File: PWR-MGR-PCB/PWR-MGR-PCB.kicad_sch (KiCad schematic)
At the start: 24 parts, among them J1 USB_C_Receptacle_USB2.0_14P, J2 Battery_1x2, U1 USBLC6-2SC6, U2 TLV75533PDBV, U3 BQ24074RGT, U4 TPS631011YBGR

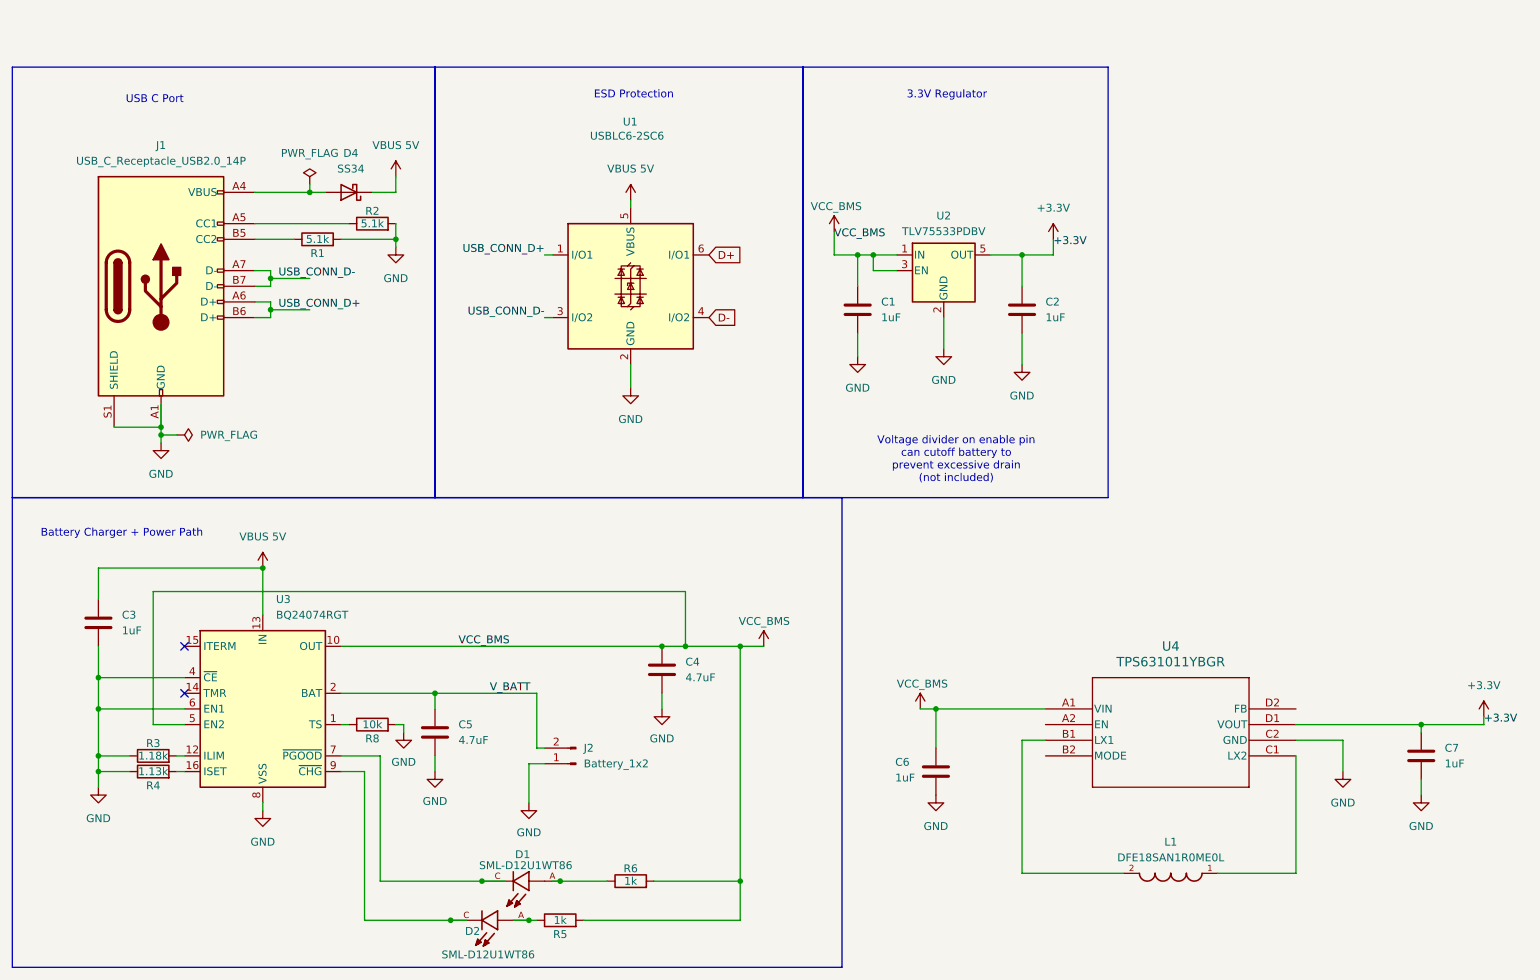
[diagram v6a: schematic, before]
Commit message: Configure buck boost converter
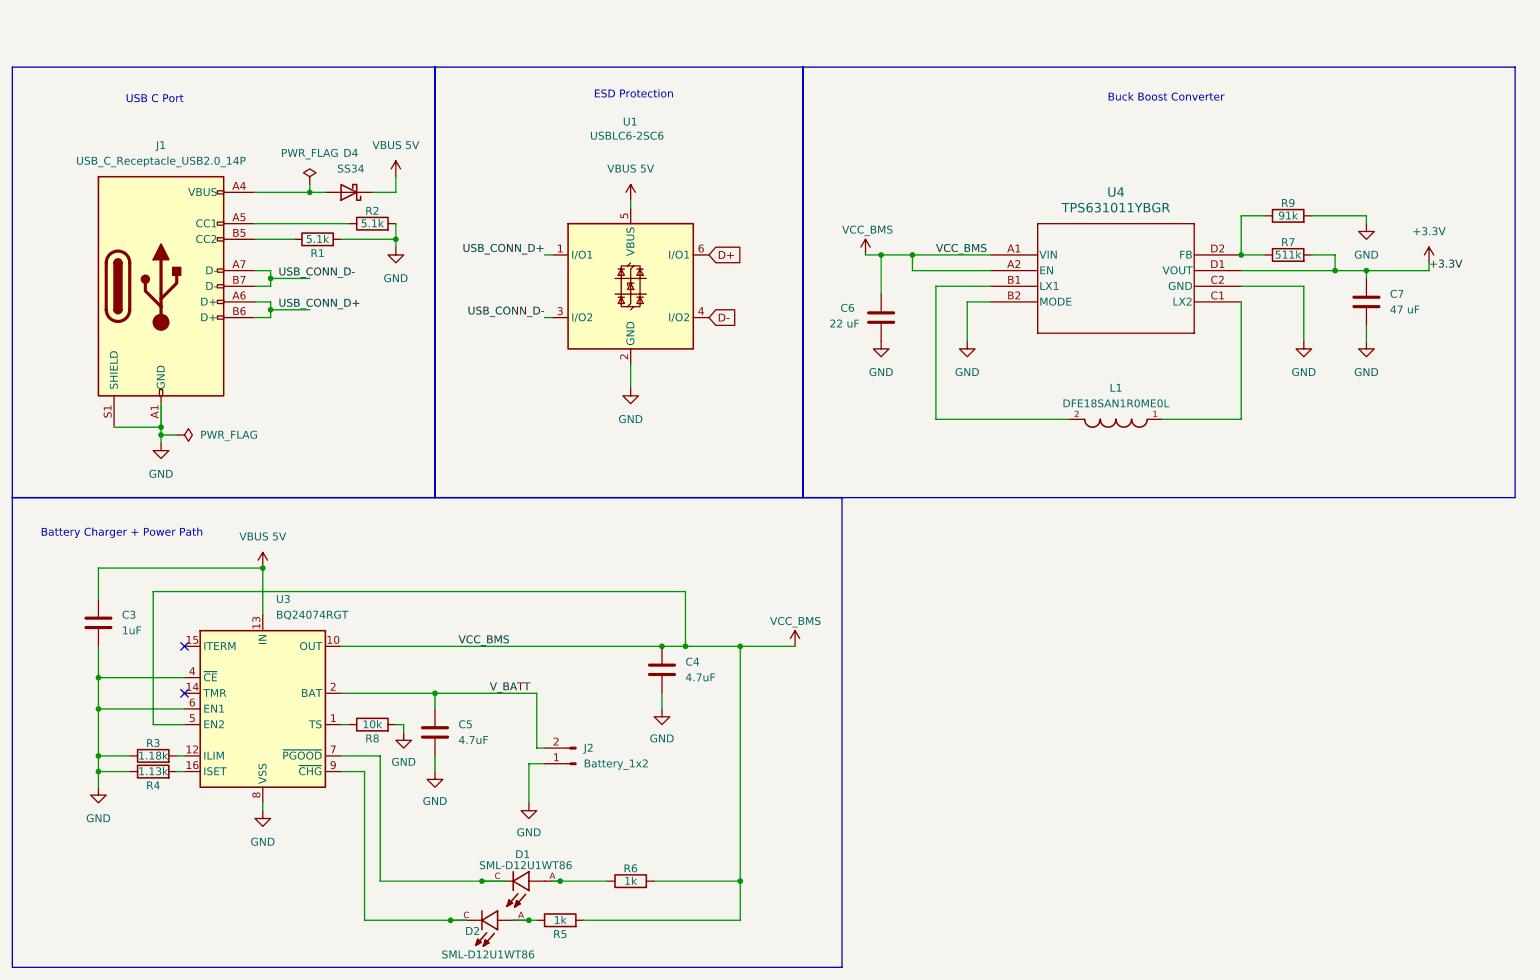
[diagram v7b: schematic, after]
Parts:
- removed C1, C2: 1uF, Capacitor_SMD:C_0805_2012Metric, symbol Device:C
- removed U2: TLV75533PDBV, Package_TO_SOT_SMD:SOT-23-5, symbol Regulator_Linear:TLV75533PDBV
- added R7: 511k, Resistor_SMD:R_0805_2012Metric, symbol Device:R
- added R9: 91k, Resistor_SMD:R_0805_2012Metric, symbol Device:R
- C6: value 1uF -> 22 uF
- C7: value 1uF -> 47 uF
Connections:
- net +3.3V: now also R7.2
- net GND: now also U4.B2 (MODE), R9.2
- net VCC_BMS: now also U4.A2 (EN)
- net at U4.D2 (FB): now also R7.1, R9.1
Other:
- note added: "Buck Boost Converter"
- note removed: "3.3V Regulator"
- note removed: "Voltage divider on enable pin can cutoff battery to prevent excessive drain (not included)"
- moved on the sheet: C6, C7, L1, U4

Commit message: Route buck boost converter, add ground plane
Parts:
- L1: footprint DFE18SAN1R0ME0L:INDC1608X80N -> DFE18SAN1ROMEO Inductor:INDC1608X80N
- U4: footprint DSBGA8_YBG_TEX -> TPS631011 - Buck Boost Converter:DSBGA8_YBG_TEX
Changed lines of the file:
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@@
 			)
 		)
-		(property "Footprint" "DFE18SAN1R0ME0L:INDC1608X80N"
+		(property "Footprint" "DFE18SAN1ROMEO Inductor:INDC1608X80N"
 			(at 207.01 85.09 0)
 			(effects
@@
 			)
 		)
-		(property "Footprint" "DSBGA8_YBG_TEX"
+		(property "Footprint" "TPS631011 - Buck Boost Converter:DSBGA8_YBG_TEX"
 			(at 186.69 58.42 0)
 			(effects
